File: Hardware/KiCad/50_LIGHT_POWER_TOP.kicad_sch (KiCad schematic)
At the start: 0 parts

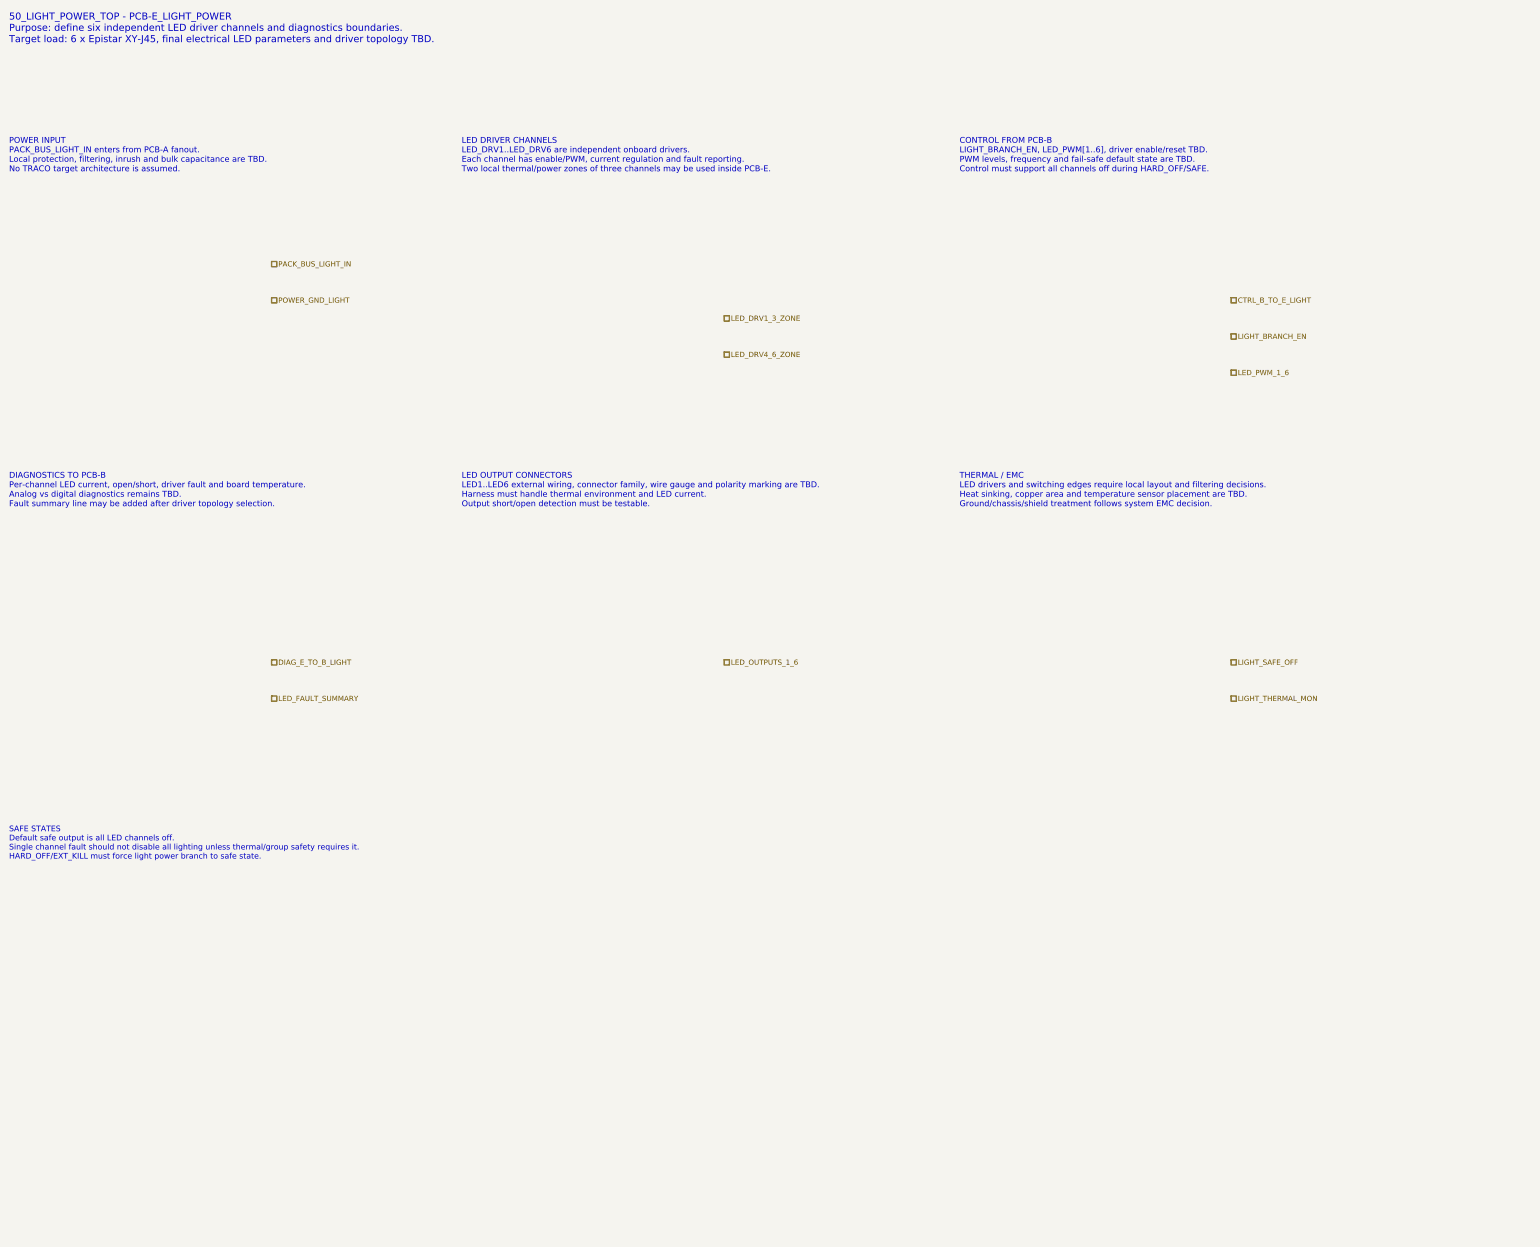
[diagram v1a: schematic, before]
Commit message: hardware: map PCB-E LIGHT_POWER detailed hierarchy
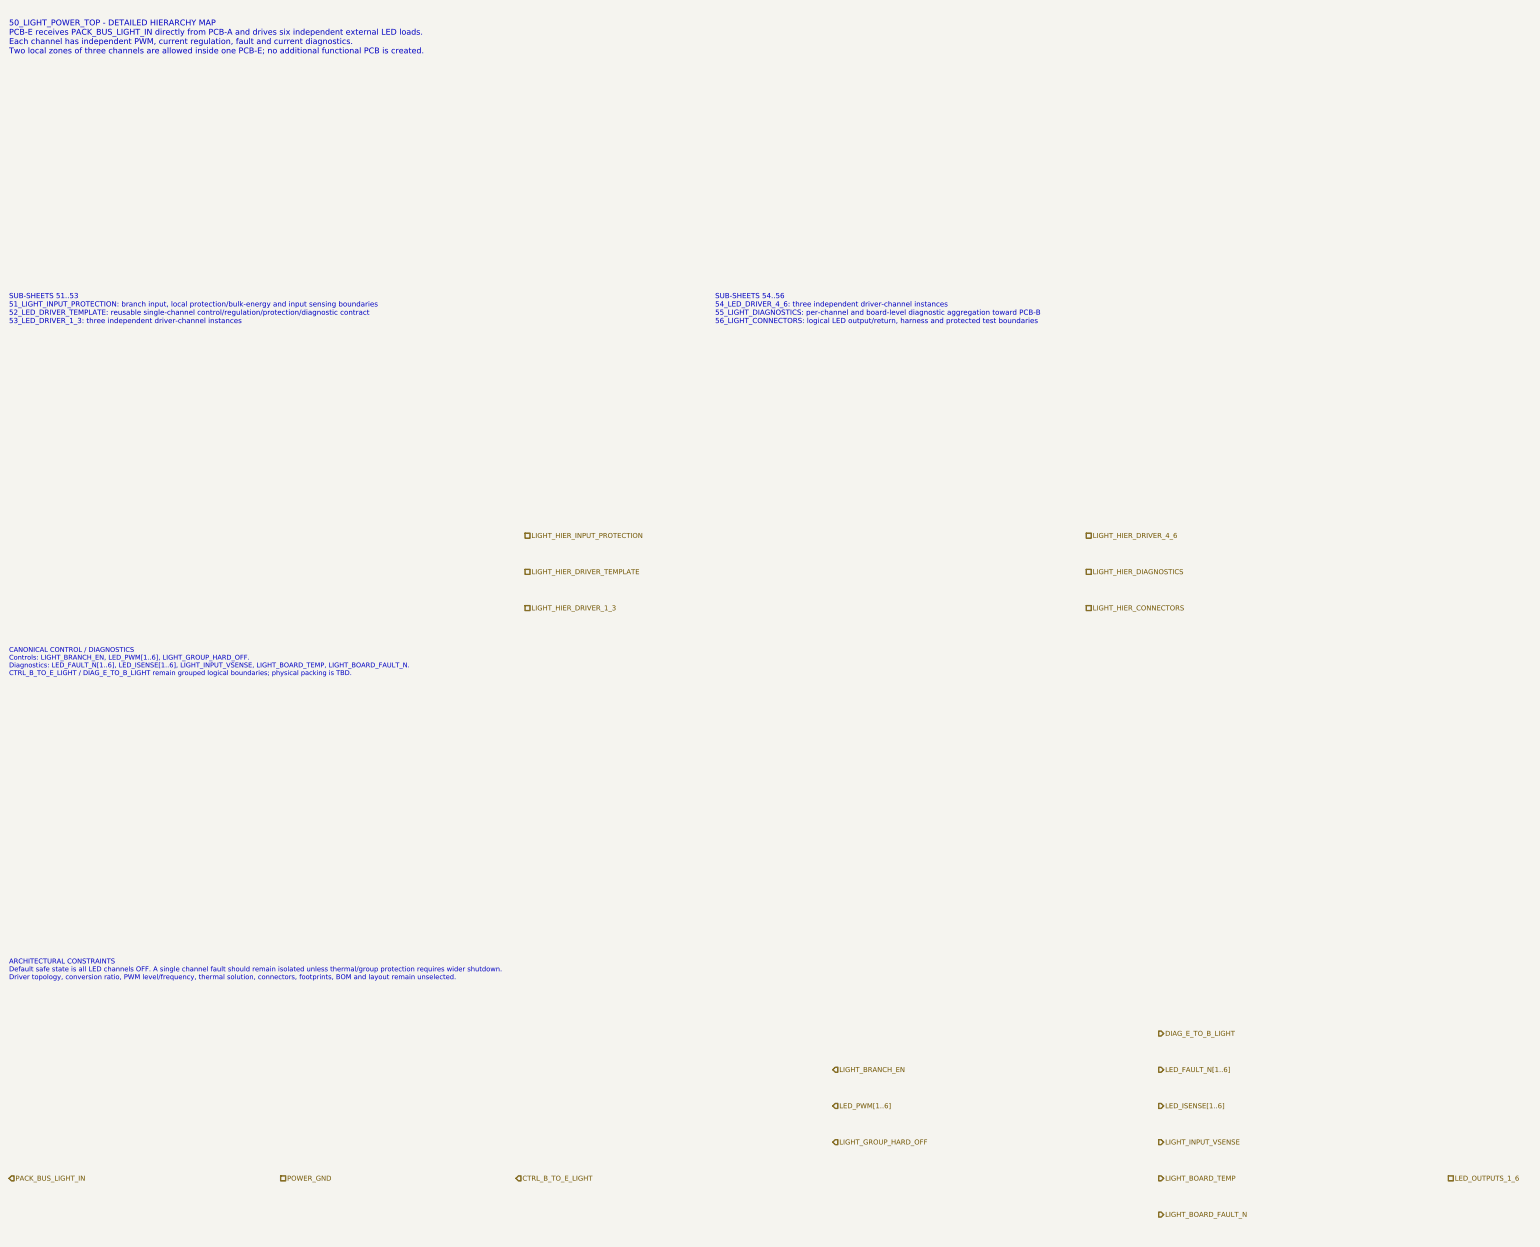
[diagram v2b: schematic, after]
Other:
- note added: "50_LIGHT_POWER_TOP - DETAILED HIERARCHY MAP PCB-E receives PACK_BUS_LIGHT_IN directly from PCB-A and drives six independent external LED loads. Each channel has independent PWM, current regulation, fault and current diagnostics. Two local zones of three channels are allowed inside one PCB-E; no additional functional PCB is created."
- note added: "ARCHITECTURAL CONSTRAINTS Default safe state is all LED channels OFF. A single channel fault should remain isolated unless thermal/group protection requires wider shutdown. Driver topology, conversion ratio, PWM level/frequency, thermal solution, connectors, footprints, BOM and layout remain unselected."
- note added: "CANONICAL CONTROL / DIAGNOSTICS Controls: LIGHT_BRANCH_EN, LED_PWM[1..6], LIGHT_GROUP_HARD_OFF. Diagnostics: LED_FAULT_N[1..6], LED_ISENSE[1..6], LIGHT_INPUT_VSENSE, LIGHT_BOARD_TEMP, LIGHT_BOARD_FAULT_N. CTRL_B_TO_E_LIGHT / DIAG_E_TO_B_LIGHT remain grouped logical boundaries; physical packing is TBD."
- note added: "SUB-SHEETS 51..53 51_LIGHT_INPUT_PROTECTION: branch input, local protection/bulk-energy and input sensing boundaries 52_LED_DRIVER_TEMPLATE: reusable single-channel control/regulation/protection/diagnostic contract 53_LED_DRIVER_1_3: three independent driver-channel instances"
- note added: "SUB-SHEETS 54..56 54_LED_DRIVER_4_6: three independent driver-channel instances 55_LIGHT_DIAGNOSTICS: per-channel and board-level diagnostic aggregation toward PCB-B 56_LIGHT_CONNECTORS: logical LED output/return, harness and protected test boundaries"
- note removed: "50_LIGHT_POWER_TOP - PCB-E_LIGHT_POWER Purpose: define six independent LED driver channels and diagnostics boundaries. Target load: 6 x Epistar XY-J45, final electrical LED parameters and driver topology TBD."
- note removed: "CONTROL FROM PCB-B LIGHT_BRANCH_EN, LED_PWM[1..6], driver enable/reset TBD. PWM levels, frequency and fail-safe default state are TBD. Control must support all channels off during HARD_OFF/SAFE."
- note removed: "DIAGNOSTICS TO PCB-B Per-channel LED current, open/short, driver fault and board temperature. Analog vs digital diagnostics remains TBD. Fault summary line may be added after driver topology selection."
- note removed: "LED DRIVER CHANNELS LED_DRV1..LED_DRV6 are independent onboard drivers. Each channel has enable/PWM, current regulation and fault reporting. Two local thermal/power zones of three channels may be used inside PCB-E."
- note removed: "LED OUTPUT CONNECTORS LED1..LED6 external wiring, connector family, wire gauge and polarity marking are TBD. Harness must handle thermal environment and LED current. Output short/open detection must be testable."
- note removed: "POWER INPUT PACK_BUS_LIGHT_IN enters from PCB-A fanout. Local protection, filtering, inrush and bulk capacitance are TBD. No TRACO target architecture is assumed."
- note removed: "SAFE STATES Default safe output is all LED channels off. Single channel fault should not disable all lighting unless thermal/group safety requires it. HARD_OFF/EXT_KILL must force light power branch to safe state."
- note removed: "THERMAL / EMC LED drivers and switching edges require local layout and filtering decisions. Heat sinking, copper area and temperature sensor placement are TBD. Ground/chassis/shield treatment follows system EMC decision."

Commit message: hardware: align PCB-E top boundary to local PWM and CAN-FD
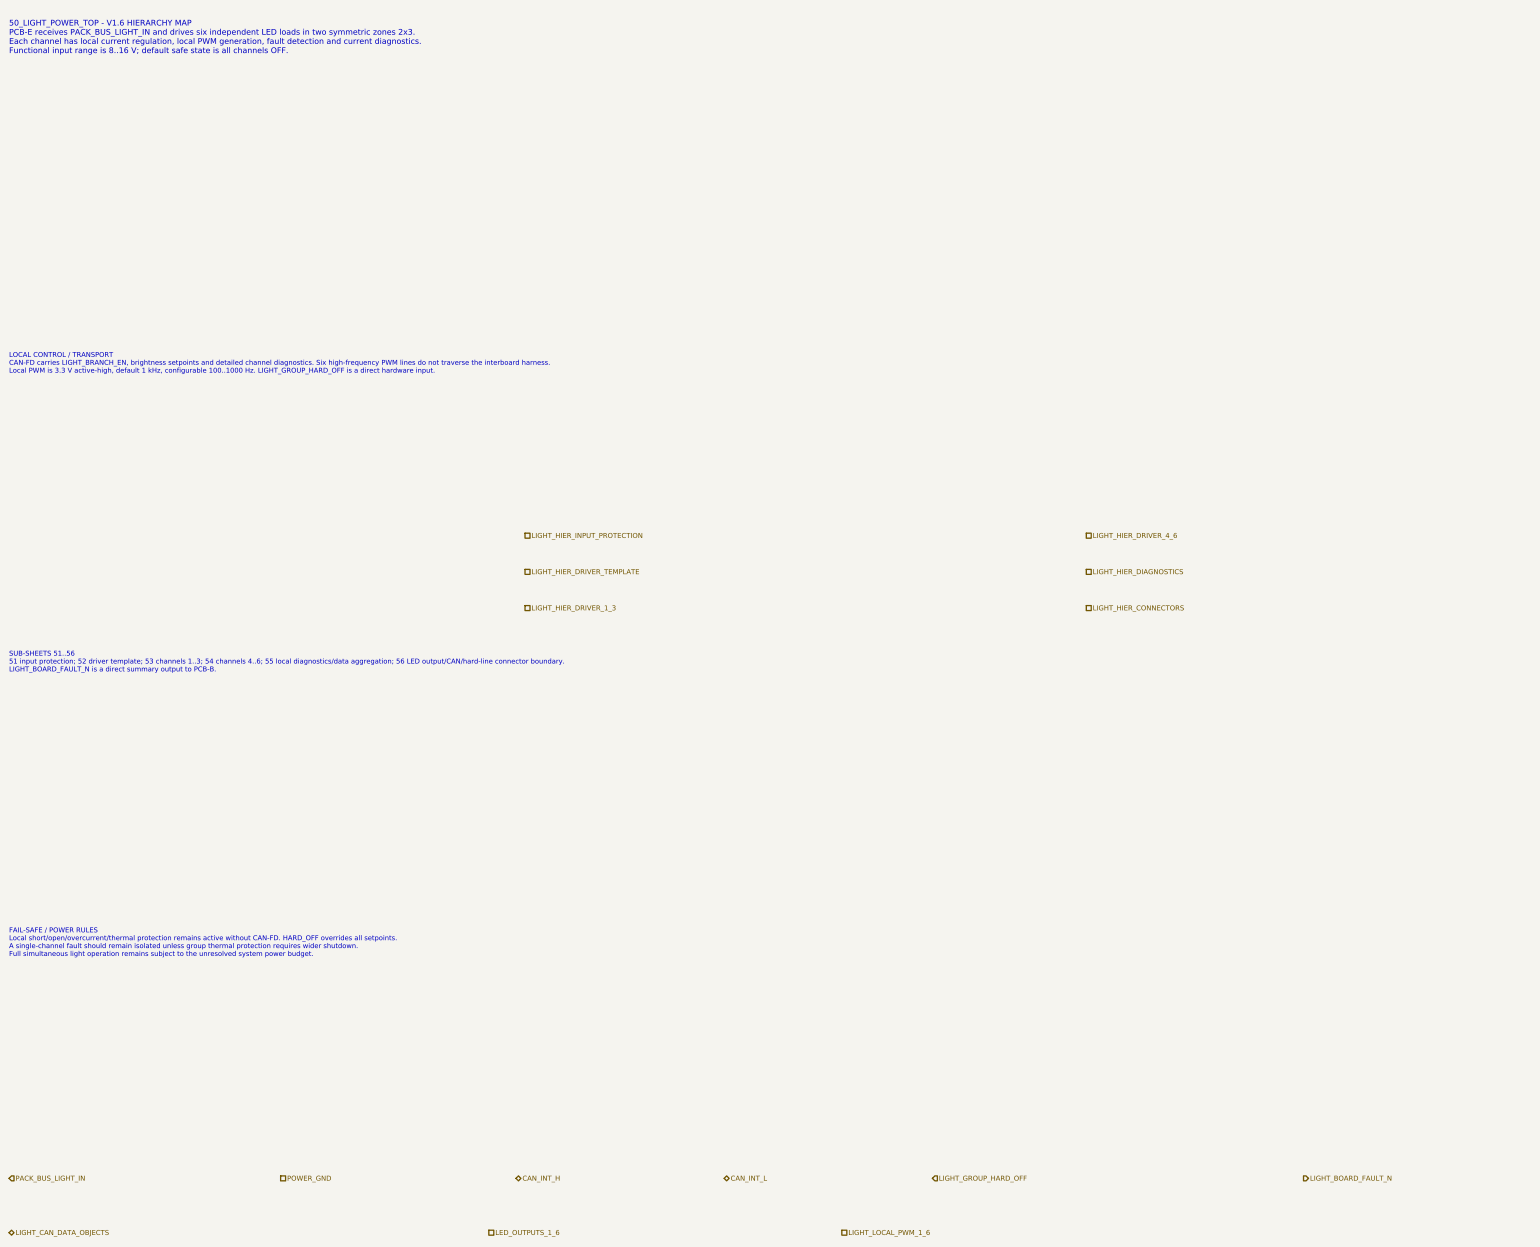
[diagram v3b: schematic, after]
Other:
- note added: "50_LIGHT_POWER_TOP - V1.6 HIERARCHY MAP PCB-E receives PACK_BUS_LIGHT_IN and drives six independent LED loads in two symmetric zones 2x3. Each channel has local current regulation, local PWM generation, fault detection and current diagnostics. Functional input range is 8..16 V; default safe state is all channels OFF."
- note added: "FAIL-SAFE / POWER RULES Local short/open/overcurrent/thermal protection remains active without CAN-FD. HARD_OFF overrides all setpoints. A single-channel fault should remain isolated unless group thermal protection requires wider shutdown. Full simultaneous light operation remains subject to the unresolved system power budget."
- note added: "LOCAL CONTROL / TRANSPORT CAN-FD carries LIGHT_BRANCH_EN, brightness setpoints and detailed channel diagnostics. Six high-frequency PWM lines do not traverse the interboard harness. Local PWM is 3.3 V active-high, default 1 kHz, configurable 100..1000 Hz. LIGHT_GROUP_HARD_OFF is a direct hardware input."
- note added: "SUB-SHEETS 51..56 51 input protection; 52 driver template; 53 channels 1..3; 54 channels 4..6; 55 local diagnostics/data aggregation; 56 LED output/CAN/hard-line connector boundary. LIGHT_BOARD_FAULT_N is a direct summary output to PCB-B."
- note removed: "50_LIGHT_POWER_TOP - DETAILED HIERARCHY MAP PCB-E receives PACK_BUS_LIGHT_IN directly from PCB-A and drives six independent external LED loads. Each channel has independent PWM, current regulation, fault and current diagnostics. Two local zones of three channels are allowed inside one PCB-E; no additional functional PCB is created."
- note removed: "ARCHITECTURAL CONSTRAINTS Default safe state is all LED channels OFF. A single channel fault should remain isolated unless thermal/group protection requires wider shutdown. Driver topology, conversion ratio, PWM level/frequency, thermal solution, connectors, footprints, BOM and layout remain unselected."
- note removed: "CANONICAL CONTROL / DIAGNOSTICS Controls: LIGHT_BRANCH_EN, LED_PWM[1..6], LIGHT_GROUP_HARD_OFF. Diagnostics: LED_FAULT_N[1..6], LED_ISENSE[1..6], LIGHT_INPUT_VSENSE, LIGHT_BOARD_TEMP, LIGHT_BOARD_FAULT_N. CTRL_B_TO_E_LIGHT / DIAG_E_TO_B_LIGHT remain grouped logical boundaries; physical packing is TBD."
- note removed: "SUB-SHEETS 51..53 51_LIGHT_INPUT_PROTECTION: branch input, local protection/bulk-energy and input sensing boundaries 52_LED_DRIVER_TEMPLATE: reusable single-channel control/regulation/protection/diagnostic contract 53_LED_DRIVER_1_3: three independent driver-channel instances"
- note removed: "SUB-SHEETS 54..56 54_LED_DRIVER_4_6: three independent driver-channel instances 55_LIGHT_DIAGNOSTICS: per-channel and board-level diagnostic aggregation toward PCB-B 56_LIGHT_CONNECTORS: logical LED output/return, harness and protected test boundaries"
